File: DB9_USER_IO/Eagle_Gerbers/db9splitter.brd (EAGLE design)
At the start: 62.5 x 19.8 mm, 17 parts, among them IC1 74LVC1G04DBV

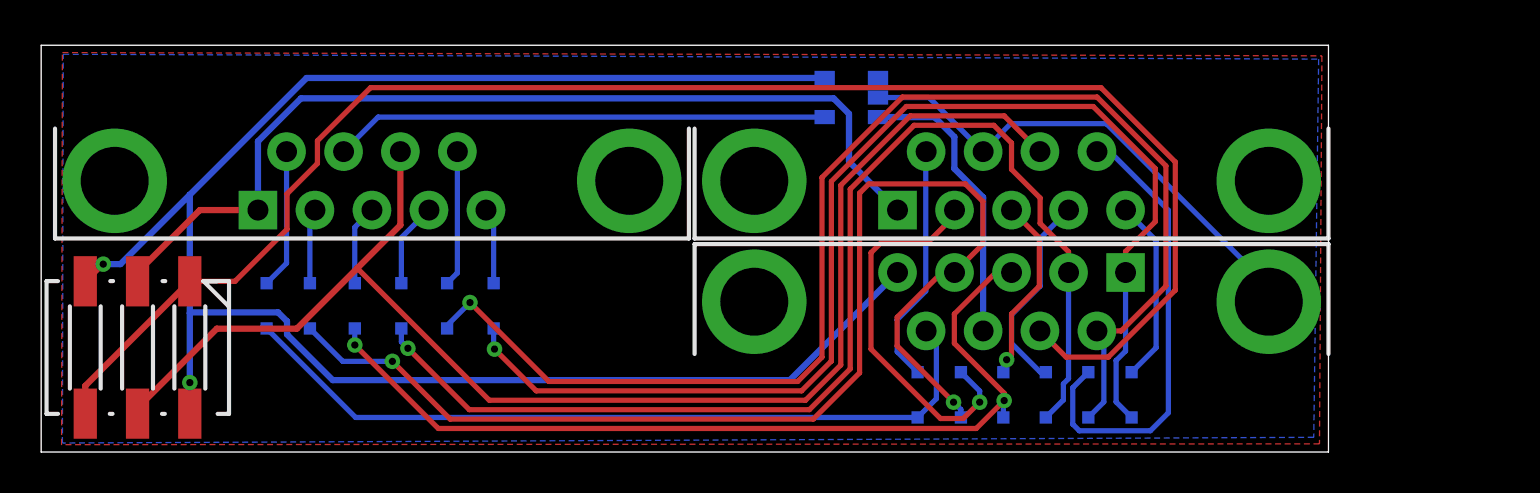
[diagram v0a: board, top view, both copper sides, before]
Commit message: Change splitter by 74HC157 circuit
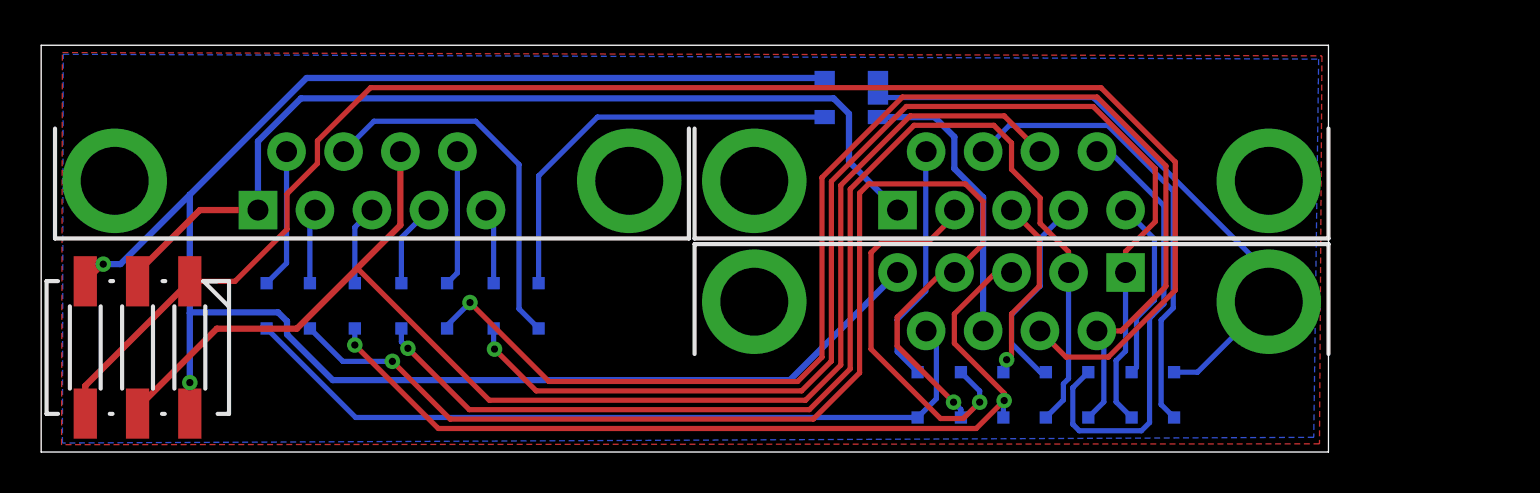
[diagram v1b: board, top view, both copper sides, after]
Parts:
- added D10, D4: (no value), diode:SOD323-R
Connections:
- new net N$15: D4.A, J1.8
- new net N$9: D10.A, J3.8
- net /SELECT: now also D10.C; no longer J3.8
- net SELECT: now also D4.C; no longer J1.8
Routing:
- net N$15: track 0.00 -> 22.6 mm
- net N$9: track 0.00 -> 18.4 mm
- net SELECT: track 24.7 -> 29.9 mm
- net /SELECT: track 24.1 -> 20.3 mm
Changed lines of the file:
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@@
 <attribute name="OC_NEWARK" value="unknown" x="18.653125" y="-9.525" size="1.778" layer="27" rot="R180" display="off"/>
+</element>
+<element name="D4" library="diode" package="SOD323-R" value="" x="55.0465625" y="2.778125" smashed="yes" rot="MR270">
+<attribute name="VALUE" x="57.3465625" y="3.878125" size="1.27" layer="28" rot="MR270"/>
+</element>
+<element name="D10" library="diode" package="SOD323-R" value="" x="24.1696875" y="7.1040625" smashed="yes" rot="MR270">
+<attribute name="VALUE" x="26.4696875" y="8.2040625" size="1.27" layer="28" rot="MR270"/>
 </element>
 </elements>
@@
 <signal name="SELECT">
 <contactref element="IC1" pad="2"/>
-<contactref element="J1" pad="8"/>
 <contactref element="J2" pad="G1"/>
-<wire x1="40.66" y1="17.224375" x2="43.140625" y2="17.224375" width="0.254" layer="16"/>
-<wire x1="43.140625" y1="17.224375" x2="45.75984375" y2="14.60515625" width="0.254" layer="16"/>
-<wire x1="45.75984375" y1="14.60515625" x2="45.76875" y2="14.59625" width="0.254" layer="16"/>
-<wire x1="59.64875" y1="7.3025" x2="59.64875" y2="8.058125" width="0.254" layer="16"/>
-<wire x1="47.1090625" y1="15.954375" x2="45.75984375" y2="14.60515625" width="0.254" layer="16"/>
-<wire x1="59.64875" y1="8.058125" x2="51.7525" y2="15.954375" width="0.254" layer="16"/>
-<wire x1="51.7525" y1="15.954375" x2="47.1090625" y2="15.954375" width="0.254" layer="16"/>
+<wire x1="59.64875" y1="7.3025" x2="59.64875" y2="7.3421875" width="0.254" layer="16"/>
+<contactref element="D4" pad="C"/>
+<wire x1="55.0465625" y1="3.878125" x2="56.1846875" y2="3.878125" width="0.254" layer="16"/>
+<wire x1="56.1846875" y1="3.878125" x2="59.64875" y2="7.3421875" width="0.254" layer="16"/>
+<wire x1="40.66" y1="17.224375" x2="51.1132625" y2="17.224375" width="0.254" layer="16"/>
+<wire x1="51.1132625" y1="17.224375" x2="59.64875" y2="8.6888875" width="0.254" layer="16"/>
+<wire x1="59.64875" y1="8.6888875" x2="59.64875" y2="7.3421875" width="0.254" layer="16"/>
 </signal>
 <signal name="/SELECT">
 <contactref element="IC1" pad="4"/>
-<contactref element="J3" pad="8"/>
-<wire x1="38.07" y1="16.274375" x2="16.3715625" y2="16.274375" width="0.254" layer="16"/>
-<wire x1="16.3715625" y1="16.274375" x2="14.6934375" y2="14.59625" width="0.254" layer="16"/>
+<wire x1="38.07" y1="16.274375" x2="27.0271875" y2="16.274375" width="0.254" layer="16"/>
+<contactref element="D10" pad="C"/>
+<wire x1="24.1696875" y1="8.2040625" x2="24.1696875" y2="13.416875" width="0.254" layer="16"/>
+<wire x1="24.1696875" y1="13.416875" x2="27.0271875" y2="16.274375" width="0.254" layer="16"/>
 </signal>
 <signal name="N$3">
@@
 <wire x1="50.1253125" y1="1.349375" x2="50.1253125" y2="3.1240625" width="0.254" layer="16"/>
 <wire x1="50.1253125" y1="3.1240625" x2="50.879375" y2="3.878125" width="0.254" layer="16"/>
-<wire x1="51.92" y1="14.59625" x2="54.76875" y2="11.7475" width="0.254" layer="16"/>
-<wire x1="54.76875" y1="1.905" x2="54.76875" y2="11.7475" width="0.254" layer="16"/>
-<wire x1="50.4428125" y1="1.031875" x2="53.895625" y2="1.031875" width="0.254" layer="16"/>
-<wire x1="53.895625" y1="1.031875" x2="54.76875" y2="1.905" width="0.254" layer="16"/>
+<wire x1="51.92" y1="14.59625" x2="54.5512625" y2="11.9649875" width="0.254" layer="16"/>
+<wire x1="53.4590625" y1="1.031875" x2="50.4428125" y2="1.031875" width="0.254" layer="16"/>
+<wire x1="54.5512625" y1="7.19249375" x2="53.980790625" y2="6.622021875" width="0.254" layer="16"/>
+<wire x1="54.5512625" y1="11.9649875" x2="54.5512625" y2="7.19249375" width="0.254" layer="16"/>
+<wire x1="53.980790625" y1="6.622021875" x2="53.8559375" y2="6.49716875" width="0.254" layer="16"/>
+<wire x1="53.8559375" y1="1.42875" x2="53.4590625" y2="1.031875" width="0.254" layer="16"/>
+<wire x1="53.8559375" y1="6.49716875" x2="53.8559375" y2="1.42875" width="0.254" layer="16"/>
 </signal>
 <signal name="N$13">
@@
 <contactref element="D13" pad="C"/>
 <contactref element="J1" pad="1"/>
-<wire x1="52.9828125" y1="3.878125" x2="54.1734375" y2="5.06875" width="0.254" layer="16"/>
-<wire x1="54.1734375" y1="10.2715625" x2="52.68875" y2="11.75625" width="0.254" layer="16"/>
-<wire x1="54.1734375" y1="5.06875" x2="54.1734375" y2="10.2715625" width="0.254" layer="16"/>
+<wire x1="54.0940625" y1="10.3509375" x2="52.68875" y2="11.75625" width="0.254" layer="16"/>
+<wire x1="52.9828125" y1="3.878125" x2="53.2209375" y2="4.11625" width="0.254" layer="16"/>
+<wire x1="53.2209375" y1="6.50875" x2="54.0940625" y2="7.381875" width="0.254" layer="16"/>
+<wire x1="54.0940625" y1="7.381875" x2="54.0940625" y2="10.3509375" width="0.254" layer="16"/>
+<wire x1="53.2209375" y1="4.11625" x2="53.2209375" y2="6.50875" width="0.254" layer="16"/>
 </signal>
 <signal name="N$2">
@@
 <wire x1="37.138625" y1="2.5146" x2="21.77415" y2="2.5146" width="0.254" layer="1"/>
 </signal>
+<signal name="N$9">
+<contactref element="J3" pad="8"/>
+<contactref element="D10" pad="A"/>
+<wire x1="24.1696875" y1="6.0040625" x2="23.2171875" y2="6.9565625" width="0.254" layer="16"/>
+<wire x1="23.2171875" y1="13.97" x2="21.11375" y2="16.0734375" width="0.254" layer="16"/>
+<wire x1="21.11375" y1="16.0734375" x2="16.170625" y2="16.0734375" width="0.254" layer="16"/>
+<wire x1="16.170625" y1="16.0734375" x2="14.6934375" y2="14.59625" width="0.254" layer="16"/>
+<wire x1="23.2171875" y1="6.9565625" x2="23.2171875" y2="13.97" width="0.254" layer="16"/>
+</signal>
+<signal name="N$15">
+<contactref element="J1" pad="8"/>
+<contactref element="D4" pad="A"/>
+<wire x1="55.0465625" y1="1.678125" x2="54.4163625" y2="2.308325" width="0.254" layer="16"/>
+<wire x1="54.4163625" y1="6.41100625" x2="55.0084625" y2="7.00310625" width="0.254" layer="16"/>
+<wire x1="54.4163625" y1="2.308325" x2="54.4163625" y2="6.41100625" width="0.254" layer="16"/>
+<wire x1="55.0084625" y1="12.68259375" x2="51.82480625" y2="15.86625" width="0.254" layer="16"/>
+<wire x1="47.03875" y1="15.86625" x2="45.76875" y2="14.59625" width="0.254" layer="16"/>
+<wire x1="55.0084625" y1="7.00310625" x2="55.0084625" y2="12.68259375" width="0.254" layer="16"/>
+<wire x1="51.82480625" y1="15.86625" x2="47.03875" y2="15.86625" width="0.254" layer="16"/>
+</signal>
 </signals>

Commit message: updated db9splitter
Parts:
- removed D1, D10, D11, D12, D13, D14, D2, D3, D4, D5, D6, D7, D8, D9: (no value), diode:SOD323-R
- removed IC1: 74LVC1G04DBV, 74xx-little-de:SOT23-5
- added IC2, IC3: 74HC157D, 74xx-eu:SO16
- added RN2, RN3, RN5: 10K, resistor-dil:0603-ARC
- moved J1 8.18 mm to (55.3, 13.2)
- moved J2 8.18 mm to (55.3, 7.30)
- moved J3 8.18 mm to (24.2, 13.2)
- moved S1 8.18 mm to (12.9, 5.08)
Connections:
- removed net /SELECT: D10.C, IC1.4
- removed net N$1: D13.C, J1.1
- removed net N$11: D6.C, J1.9
- removed net N$12: D5.C, J1.6
- removed net N$13: D12.C, J3.9
- removed net N$14: D11.C, J3.6
- removed net N$15: D4.A, J1.8
- removed net N$2: D14.C, J3.1
- removed net N$3: D2.C, J1.3
- removed net N$4: D8.C, J3.3
- removed net N$5: D1.C, J1.2
- removed net N$6: D3.C, J1.4
- removed net N$7: D7.C, J3.2
- removed net N$8: D9.C, J3.4
- removed net N$9: D10.A, J3.8
- new net 1PDOWN: IC2.14, J1.2, RN2.1
- new net 1PFIRE1: IC3.11, J1.6, RN5.1
- new net 1PFIRE2: IC3.5, J1.9, RN5.3
- new net 1PLEFT: IC2.5, J1.3, RN5.2
- new net 1PRIGHT: IC2.2, J1.4, RN5.4
- new net 1PUP: IC2.11, J1.1, RN2.2
- new net 2PDOWN: IC2.13, J3.2, RN3.1
- new net 2PFIRE1: IC3.10, J3.6, RN2.4
- new net 2PFIRE2: IC3.6, J3.9, RN3.4
- new net 2PLEFT: IC2.6, J3.3, RN3.2
- new net 2PRIGHT: IC2.3, J3.4, RN3.3
- new net 2PUP: IC2.10, J3.1, RN2.3
- net DOWN: now also IC2.12; no longer D1.A, D7.A
- net FIRE1: now also IC3.9; no longer D11.A, D5.A
- net FIRE2: now also IC3.7; no longer D12.A, D6.A
- net GND: now also IC2.15, IC2.8, IC3.15, IC3.8, J1.8, J3.8; no longer IC1.3
- net LEFT: now also IC2.7; no longer D2.A, D8.A
- net RIGHT: now also IC2.4; no longer D3.A, D9.A
- net SELECT: now also IC2.1, IC3.1; no longer D4.C, IC1.2
- net UP: now also IC2.9; no longer D13.A, D14.A
- net VCC: now also IC2.16, IC3.16, RN2.5, RN2.6, RN2.7, RN2.8, RN3.5, RN3.6, RN3.7, RN3.8, RN5.5, RN5.6, RN5.7, RN5.8; no longer IC1.5
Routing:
- net GND: track 14.1 -> 73.1 mm, vias 0 -> 4
- net 1PFIRE1: track 0.00 -> 54.5 mm, vias 0 -> 1
- net 1PRIGHT: track 0.00 -> 54.5 mm
- net 1PLEFT: track 0.00 -> 44.9 mm, vias 0 -> 1
- net 1PUP: track 0.00 -> 44.5 mm, vias 0 -> 2
- net 1PFIRE2: track 0.00 -> 41.4 mm, vias 0 -> 1
- net 2PRIGHT: track 0.00 -> 41.3 mm, vias 0 -> 1
- net 1PDOWN: track 0.00 -> 38.2 mm, vias 0 -> 2
- net RIGHT: track 58.6 -> 26.2 mm, vias 2 -> 1
- net PIN5: track 46.4 -> 78.3 mm
- net 2PDOWN: track 0.00 -> 30.0 mm
- net DOWN: track 57.8 -> 33.4 mm, vias 1 -> 0
- net UP: track 59.3 -> 35.3 mm, vias 1 -> 0
- net 2PFIRE1: track 0.00 -> 23.7 mm
- net N$15: track 22.6 -> 0.00 mm
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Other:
- board size 62.5 x 19.8 mm -> 70.7 x 20 mm
